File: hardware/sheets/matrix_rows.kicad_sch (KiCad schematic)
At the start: 0 parts

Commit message: hw: draw LED matrix, row and column drivers and scan-stall safety (#8)
* repo: ignore KiCad local history

KiCad 10 keeps automatic snapshots in a .history folder (with its own
Git repository) next to the project. Ignore it, and make the hygiene
check reject it, so local history cannot be committed.

* hw: save schematic sheets in KiCad's own format

Opening and saving the project in KiCad 10 rewrites the generated
sheets and project file in its native layout. KiCad also merges seven
overlapping wire segments on the USB sheet. Nets, values and
footprints are unchanged, so committing this once keeps later edits
made in KiCad free of formatting churn.

* hw: add column driver and monostable symbols

Add a TLC59283 symbol with the RGE (VQFN-24) pin numbers from TI's pin
table; it uses KiCad's footprint for TI's RGE0024C package. Add a
single-unit SN74LVC1G123 symbol, because KiCad's version keeps the
supply pins in a separate unit.

* hw: draw matrix driver and LED matrix sheets

Columns: two cascaded TLC59283 sinks on 3V3. R_IREF is 2.94k, an
18.0 mA nominal setting (about 19.4 mA worst case with driver and
resistor tolerance), with a fitted 0 ohm in series, so adjustment can
only lower the current.

Rows: the TLC chain output, clock, latch and SAFE cross into the LED
rail through an SN74LVC8T245 translator. Four SN74HC595 on VLED drive
32 AO3401A high-side switches with 10k gate pull-ups, with row
pull-downs as unfitted options.

Scan-stall safety: every latch retriggers an SN74LVC1G123. TI
specifies 1.0-1.1 ms at 10k / 0.1 uF; with the fitted parts'
tolerances the timeout is 0.76-1.41 ms. The part has only a Q
output, so an inverter makes SAFE = NOT Q. SAFE forces the column
BLANK through an OR gate and tri-states the row registers, and the
MCU reads it. The matrix stays dark while the MCU is off or in
reset.

LED matrix: 1024 LEDs, anodes on the rows and cathodes on the
columns, drawn as row and column buses, on the front side with the
buttons (ADR 0008).

The pend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
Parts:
- added C701, C702, C703, C704, C705, C706, C709, C710, C711, C712: 100nF, Capacitor_SMD:C_0402_1005Metric, symbol Device:C
- added C707, C708: 10uF 25V, Capacitor_SMD:C_0805_2012Metric, symbol Device:C
- added Q701, Q702, Q703, Q704, Q705, Q706, Q707, Q708, Q709, Q710, Q711, Q712, Q713, Q714, Q715, Q716, Q717, Q718, Q719, Q720, Q721, Q722, Q723, Q724, Q725, Q726, Q727, Q728, Q729, Q730, Q731, Q732: AO3401A, Package_TO_SOT_SMD:SOT-23, symbol Transistor_FET:AO3401A
- added R701: 0, Resistor_SMD:R_0402_1005Metric, symbol Device:R
- added R702: 10k, Resistor_SMD:R_0402_1005Metric, symbol Device:R
- added R703, R704, R705: 100k, Resistor_SMD:R_0402_1005Metric, symbol Device:R
- added RN701, RN702, RN703, RN704, RN705, RN706, RN707, RN708: 4x10k, Resistor_SMD:R_Array_Convex_4x0603, symbol Device:R_Pack04
- added RN709, RN710, RN711, RN712, RN713, RN714, RN715, RN716: DNP, Resistor_SMD:R_Array_Convex_4x0603, symbol Device:R_Pack04
- added TP701: MTX_BLANK, TestPoint:TestPoint_Pad_D1.0mm, symbol Connector:TestPoint
- added TP702: BLANK_TLC, TestPoint:TestPoint_Pad_D1.0mm, symbol Connector:TestPoint
- added TP703: MTX_SAFE_SENSE, TestPoint:TestPoint_Pad_D1.0mm, symbol Connector:TestPoint
- added TP704: SCAN_OK, TestPoint:TestPoint_Pad_D1.0mm, symbol Connector:TestPoint
- added TP705: SER_V, TestPoint:TestPoint_Pad_D1.0mm, symbol Connector:TestPoint
- added TP706: SRCLK_V, TestPoint:TestPoint_Pad_D1.0mm, symbol Connector:TestPoint
- added TP707: RCLK_V, TestPoint:TestPoint_Pad_D1.0mm, symbol Connector:TestPoint
- added TP708: ROW0, TestPoint:TestPoint_Pad_D1.0mm, symbol Connector:TestPoint
- added TP709: ROW16, TestPoint:TestPoint_Pad_D1.0mm, symbol Connector:TestPoint
- added TP710: ROW31, TestPoint:TestPoint_Pad_D1.0mm, symbol Connector:TestPoint
- added U701: SN74LVC8T245, Package_SO:TSSOP-24_4.4x7.8mm_P0.65mm, symbol Logic_LevelTranslator:SN74LVC8T245
- added U702, U703, U704, U705: SN74HC595, Package_SO:TSSOP-16_4.4x5mm_P0.65mm, symbol 74xx:74HC595
- added U706: SN74LVC1G123, Package_SO:SSOP-8_2.95x2.8mm_P0.65mm, symbol smart-led-badge:SN74LVC1G123
- added U707: SN74LVC1G04, Package_TO_SOT_SMD:SOT-23-5, symbol 74xGxx:74LVC1G04
- added U708: SN74LVC1G32, Package_TO_SOT_SMD:SOT-23-5, symbol 74xGxx:74LVC1G32
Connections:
- new net +3V3: C701.1, C710.1, C711.1, C712.1, R702.2, R704.2, U701.1 (V_{CCA}), U701.2 (DIR), U706.8 (VCC), U707.5 (VCC), U708.5 (VCC)
- new net BLANK_TLC: TP702.1, U708.4
- new net GND: C701.2, C702.2, C703.2, C704.2, C705.2, C706.2, C707.2, C708.2, C710.2, C711.2, C712.2, R701.2, R703.2, RN709.5 (R4.2), RN709.6 (R3.2), RN709.7 (R2.2), RN709.8 (R1.2), RN710.5 (R4.2), RN710.6 (R3.2), RN710.7 (R2.2), RN710.8 (R1.2), RN711.5 (R4.2), RN711.6 (R3.2), RN711.7 (R2.2), RN711.8 (R1.2), RN712.5 (R4.2), RN712.6 (R3.2), RN712.7 (R2.2), RN712.8 (R1.2), RN713.5 (R4.2), RN713.6 (R3.2), RN713.7 (R2.2), RN713.8 (R1.2), RN714.5 (R4.2), RN714.6 (R3.2), RN714.7 (R2.2), RN714.8 (R1.2), RN715.5 (R4.2), RN715.6 (R3.2), RN715.7 (R2.2), RN715.8 (R1.2), RN716.5 (R4.2), RN716.6 (R3.2), RN716.7 (R2.2), RN716.8 (R1.2), U701.10 (A8), U701.11 (GND), U701.12 (GND), U701.13 (GND), U701.7 (A5), U701.8 (A6), U701.9 (A7), U702.8 (GND), U703.8 (GND), U704.8 (GND), U705.8 (GND), U706.1 (~{A}), U706.4 (GND), U707.3 (GND), U708.3 (GND)
- new net MONO_CEXT: C709.1, U706.6 (Cext)
- new net MONO_RCEXT: C709.2, R702.1, U706.7 (Rext/Cext)
- new net MTX_ARM: R703.1, U706.3 (~{CLR})
- new net MTX_BLANK: R704.1, TP701.1, U708.1
- new net MTX_LAT: U701.5 (A3), U706.2 (B)
- new net MTX_MISO: U701.3 (A1)
- new net MTX_SAFE_SENSE: TP703.1, U701.6 (A4), U707.4, U708.2
- new net MTX_SCK: U701.4 (A2)
- new net OE_V: R705.1, U701.18 (B4), U702.13 (~{OE}), U703.13 (~{OE}), U704.13 (~{OE}), U705.13 (~{OE})
- new net RCLK_V: TP707.1, U701.19 (B3), U702.12 (RCLK), U703.12 (RCLK), U704.12 (RCLK), U705.12 (RCLK)
- new net RG0: Q701.1 (G), RN701.1 (R1.1), U702.15 (QA)
- new net RG1: Q702.1 (G), RN701.2 (R2.1), U702.1 (QB)
- new net RG10: Q711.1 (G), RN703.3 (R3.1), U703.2 (QC)
- new net RG11: Q712.1 (G), RN703.4 (R4.1), U703.3 (QD)
- new net RG12: Q713.1 (G), RN704.1 (R1.1), U703.4 (QE)
- new net RG13: Q714.1 (G), RN704.2 (R2.1), U703.5 (QF)
- new net RG14: Q715.1 (G), RN704.3 (R3.1), U703.6 (QG)
- new net RG15: Q716.1 (G), RN704.4 (R4.1), U703.7 (QH)
- new net RG16: Q717.1 (G), RN705.1 (R1.1), U704.15 (QA)
- new net RG17: Q718.1 (G), RN705.2 (R2.1), U704.1 (QB)
- new net RG18: Q719.1 (G), RN705.3 (R3.1), U704.2 (QC)
- new net RG19: Q720.1 (G), RN705.4 (R4.1), U704.3 (QD)
- new net RG2: Q703.1 (G), RN701.3 (R3.1), U702.2 (QC)
- new net RG20: Q721.1 (G), RN706.1 (R1.1), U704.4 (QE)
- new net RG21: Q722.1 (G), RN706.2 (R2.1), U704.5 (QF)
- new net RG22: Q723.1 (G), RN706.3 (R3.1), U704.6 (QG)
- new net RG23: Q724.1 (G), RN706.4 (R4.1), U704.7 (QH)
- new net RG24: Q725.1 (G), RN707.1 (R1.1), U705.15 (QA)
- new net RG25: Q726.1 (G), RN707.2 (R2.1), U705.1 (QB)
- new net RG26: Q727.1 (G), RN707.3 (R3.1), U705.2 (QC)
- new net RG27: Q728.1 (G), RN707.4 (R4.1), U705.3 (QD)
- new net RG28: Q729.1 (G), RN708.1 (R1.1), U705.4 (QE)
- new net RG29: Q730.1 (G), RN708.2 (R2.1), U705.5 (QF)
- new net RG3: Q704.1 (G), RN701.4 (R4.1), U702.3 (QD)
- new net RG30: Q731.1 (G), RN708.3 (R3.1), U705.6 (QG)
- new net RG31: Q732.1 (G), RN708.4 (R4.1), U705.7 (QH)
- new net RG4: Q705.1 (G), RN702.1 (R1.1), U702.4 (QE)
- new net RG5: Q706.1 (G), RN702.2 (R2.1), U702.5 (QF)
- new net RG6: Q707.1 (G), RN702.3 (R3.1), U702.6 (QG)
- new net RG7: Q708.1 (G), RN702.4 (R4.1), U702.7 (QH)
- new net RG8: Q709.1 (G), RN703.1 (R1.1), U703.15 (QA)
- new net RG9: Q710.1 (G), RN703.2 (R2.1), U703.1 (QB)
- new net ROW0: Q701.3 (D), RN709.1 (R1.1), TP708.1
- new net ROW1: Q702.3 (D), RN709.2 (R2.1)
- new net ROW10: Q711.3 (D), RN711.3 (R3.1)
- new net ROW11: Q712.3 (D), RN711.4 (R4.1)
- new net ROW12: Q713.3 (D), RN712.1 (R1.1)
- new net ROW13: Q714.3 (D), RN712.2 (R2.1)
- new net ROW14: Q715.3 (D), RN712.3 (R3.1)
- new net ROW15: Q716.3 (D), RN712.4 (R4.1)
- new net ROW16: Q717.3 (D), RN713.1 (R1.1), TP709.1
- new net ROW17: Q718.3 (D), RN713.2 (R2.1)
- new net ROW18: Q719.3 (D), RN713.3 (R3.1)
- new net ROW19: Q720.3 (D), RN713.4 (R4.1)
- new net ROW2: Q703.3 (D), RN709.3 (R3.1)
- new net ROW20: Q721.3 (D), RN714.1 (R1.1)
- new net ROW21: Q722.3 (D), RN714.2 (R2.1)
- new net ROW22: Q723.3 (D), RN714.3 (R3.1)
- new net ROW23: Q724.3 (D), RN714.4 (R4.1)
- new net ROW24: Q725.3 (D), RN715.1 (R1.1)
- new net ROW25: Q726.3 (D), RN715.2 (R2.1)
- new net ROW26: Q727.3 (D), RN715.3 (R3.1)
- new net ROW27: Q728.3 (D), RN715.4 (R4.1)
- new net ROW28: Q729.3 (D), RN716.1 (R1.1)
- new net ROW29: Q730.3 (D), RN716.2 (R2.1)
- new net ROW3: Q704.3 (D), RN709.4 (R4.1)
- new net ROW30: Q731.3 (D), RN716.3 (R3.1)
- new net ROW31: Q732.3 (D), RN716.4 (R4.1), TP710.1
- new net ROW4: Q705.3 (D), RN710.1 (R1.1)
- new net ROW5: Q706.3 (D), RN710.2 (R2.1)
- new net ROW6: Q707.3 (D), RN710.3 (R3.1)
- new net ROW7: Q708.3 (D), RN710.4 (R4.1)
- new net ROW8: Q709.3 (D), RN711.1 (R1.1)
- new net ROW9: Q710.3 (D), RN711.2 (R2.1)
- new net SCAN_OK: TP704.1, U706.5 (Q), U707.2
- new net SER1: U702.9 (QH'), U703.14 (SER)
- new net SER2: U703.9 (QH'), U704.14 (SER)
- new net SER3: U704.9 (QH'), U705.14 (SER)
- new net SER_V: TP705.1, U701.21 (B1), U702.14 (SER)
- new net SRCLK_V: TP706.1, U701.20 (B2), U702.11 (SRCLK), U703.11 (SRCLK), U704.11 (SRCLK), U705.11 (SRCLK)
- new net VLED: C702.1, C703.1, C704.1, C705.1, C706.1, C707.1, C708.1, Q701.2 (S), Q702.2 (S), Q703.2 (S), Q704.2 (S), Q705.2 (S), Q706.2 (S), Q707.2 (S), Q708.2 (S), Q709.2 (S), Q710.2 (S), Q711.2 (S), Q712.2 (S), Q713.2 (S), Q714.2 (S), Q715.2 (S), Q716.2 (S), Q717.2 (S), Q718.2 (S), Q719.2 (S), Q720.2 (S), Q721.2 (S), Q722.2 (S), Q723.2 (S), Q724.2 (S), Q725.2 (S), Q726.2 (S), Q727.2 (S), Q728.2 (S), Q729.2 (S), Q730.2 (S), Q731.2 (S), Q732.2 (S), R705.2, RN701.5 (R4.2), RN701.6 (R3.2), RN701.7 (R2.2), RN701.8 (R1.2), RN702.5 (R4.2), RN702.6 (R3.2), RN702.7 (R2.2), RN702.8 (R1.2), RN703.5 (R4.2), RN703.6 (R3.2), RN703.7 (R2.2), RN703.8 (R1.2), RN704.5 (R4.2), RN704.6 (R3.2), RN704.7 (R2.2), RN704.8 (R1.2), RN705.5 (R4.2), RN705.6 (R3.2), RN705.7 (R2.2), RN705.8 (R1.2), RN706.5 (R4.2), RN706.6 (R3.2), RN706.7 (R2.2), RN706.8 (R1.2), RN707.5 (R4.2), RN707.6 (R3.2), RN707.7 (R2.2), RN707.8 (R1.2), RN708.5 (R4.2), RN708.6 (R3.2), RN708.7 (R2.2), RN708.8 (R1.2), U701.23 (V_{CCB}), U701.24 (V_{CCB}), U702.10 (~{SRCLR}), U702.16 (VCC), U703.10 (~{SRCLR}), U703.16 (VCC), U704.10 (~{SRCLR}), U704.16 (VCC), U705.10 (~{SRCLR}), U705.16 (VCC)
- new net XLAT_OE_N: R701.1, U701.22 (~{OE})
- no-connect marks 0 -> 5
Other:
- note added: "Matrix row drivers and scan-stall safety (Rev A) - design notes Row chain: TLC chain SOUT (MTX_MISO), MTX_SCK, MTX_LAT and SAFE cross into the VLED domain through U701 (SN74LVC8T245, VCCA 3V3, VCCB VLED, DIR high = A to B). Its VCC isolation and Ioff keep 3V3 signals off the unpowered 595s when the LED rail is off. 4 x SN74HC595 on VLED (VCC 2-6 V) shift 32 row bits behind the 32 column bits; one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"

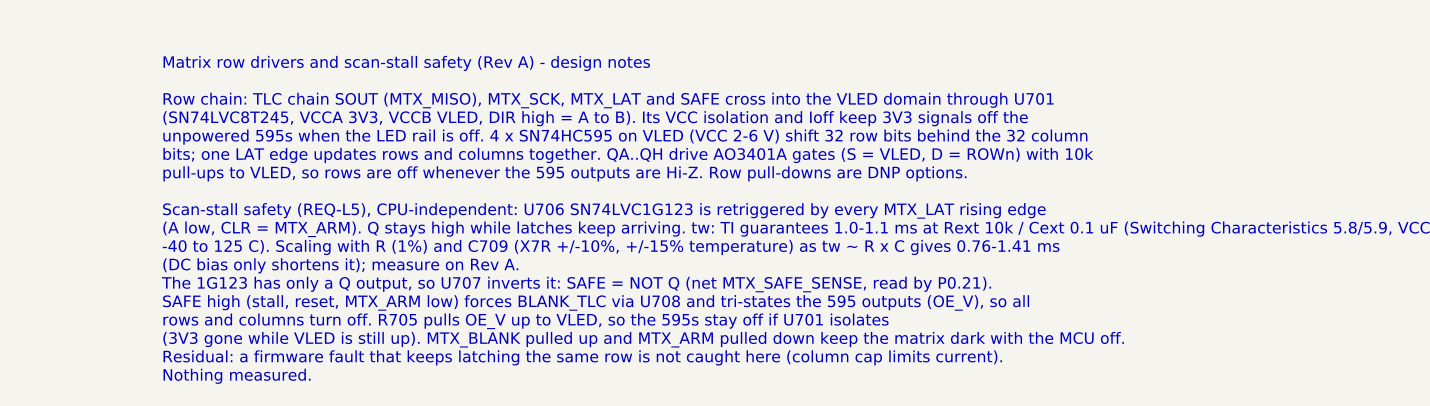
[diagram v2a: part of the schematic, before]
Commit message: hw: switch U401 to the E73 nRF52840 module
The MDBT53-P1M cannot be sourced in time for the Rev A order, while
the E73-2G4M08S1C is stocked at JLCPCB (ADR 0015).

The E73 holds its DC/DC inductors and decoupling, so L401/L402 and
C403/C404 are removed. The nRF52840 has no internal 32.768 kHz load,
so C405/C406 are fitted with 12 pF; the value is calculated and still
needs checking against the Product Specification. All 29 module GPIO
are used: CHG_STAT is no longer read by the MCU, and the UART pads,
spare GPIO pads and IMU SPI-fallback links are removed. Pins Ebyte
marks as low-frequency carry only analog inputs or slow signals.
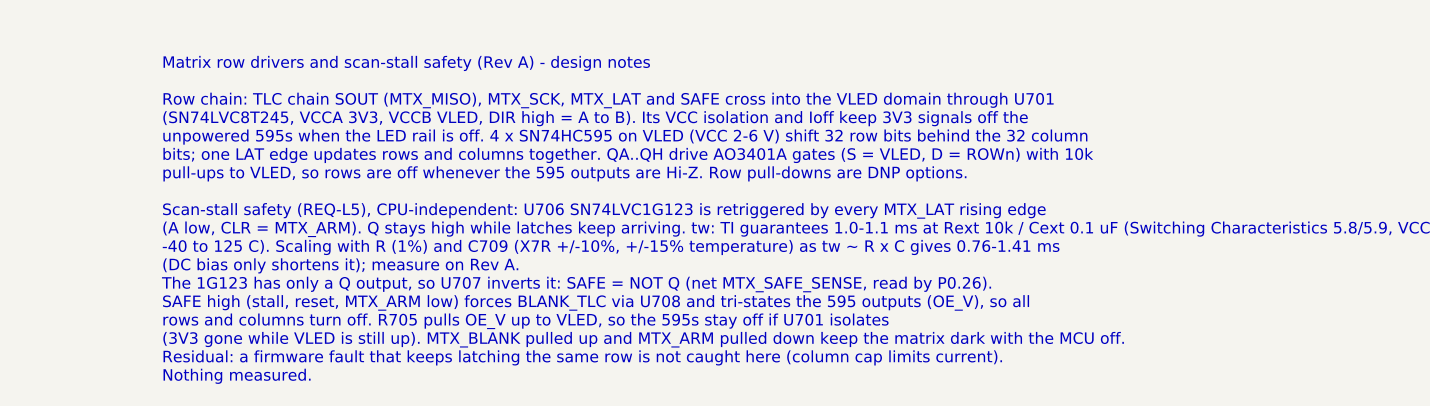
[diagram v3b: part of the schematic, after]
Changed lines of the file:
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@@
 		(comment 2 "Schematic frozen for layout after review 2026-10-07; not for fabrication until the release gate")
 	)
-	(text "Matrix row drivers and scan-stall safety (Rev A) - design notes\n\nRow chain: TLC chain SOUT (MTX_MISO), MTX_SCK, MTX_LAT and SAFE cross into the VLED domain through U701\n(SN74LVC8T245, VCCA 3V3, VCCB VLED, DIR high = A to B). Its VCC isolation and Ioff keep 3V3 signals off the\nunpowered 595s when the LED rail is off. 4 x SN74HC595 on VLED (VCC 2-6 V) shift 32 row bits behind the 32 column\nbits; one LAT edge updates rows and columns together. QA..QH drive AO3401A gates (S = VLED, D = ROWn) with 10k\npull-ups to VLED, so rows are off whenever the 595 outputs are Hi-Z. Row pull-downs are DNP options.\n\nScan-stall safety (REQ-L5), CPU-independent: U706 SN74LVC1G123 is retriggered by every MTX_LAT rising edge\n(A low, CLR = MTX_ARM). Q stays high while latches keep arriving. tw: TI guarantees 1.0-1.1 ms at Rext 10k / Cext 0.1 uF (Switching Characteristics 5.8/5.9, VCC 3.3 V,\n-40 to 125 C). Scaling with R (1%) and C709 (X7R +/-10%, +/-15% temperature) as tw ~ R x C gives 0.76-1.41 ms\n(DC bias only shortens it); measure on Rev A.\nThe 1G123 has only a Q output, so U707 inverts it: SAFE = NOT Q (net MTX_SAFE_SENSE, read by P0.21).\nSAFE high (stall, reset, MTX_ARM low) forces BLANK_TLC via U708 and tri-states the 595 outputs (OE_V), so all\nrows and columns turn off. R705 pulls OE_V up to VLED, so the 595s stay off if U701 isolates\n(3V3 gone while VLED is still up). MTX_BLANK pulled up and MTX_ARM pulled down keep the matrix dark with the MCU off.\nResidual: a firmware fault that keeps latching the same row is not caught here (column cap limits current).\nNothing measured."
+	(text "Matrix row drivers and scan-stall safety (Rev A) - design notes\n\nRow chain: TLC chain SOUT (MTX_MISO), MTX_SCK, MTX_LAT and SAFE cross into the VLED domain through U701\n(SN74LVC8T245, VCCA 3V3, VCCB VLED, DIR high = A to B). Its VCC isolation and Ioff keep 3V3 signals off the\nunpowered 595s when the LED rail is off. 4 x SN74HC595 on VLED (VCC 2-6 V) shift 32 row bits behind the 32 column\nbits; one LAT edge updates rows and columns together. QA..QH drive AO3401A gates (S = VLED, D = ROWn) with 10k\npull-ups to VLED, so rows are off whenever the 595 outputs are Hi-Z. Row pull-downs are DNP options.\n\nScan-stall safety (REQ-L5), CPU-independent: U706 SN74LVC1G123 is retriggered by every MTX_LAT rising edge\n(A low, CLR = MTX_ARM). Q stays high while latches keep arriving. tw: TI guarantees 1.0-1.1 ms at Rext 10k / Cext 0.1 uF (Switching Characteristics 5.8/5.9, VCC 3.3 V,\n-40 to 125 C). Scaling with R (1%) and C709 (X7R +/-10%, +/-15% temperature) as tw ~ R x C gives 0.76-1.41 ms\n(DC bias only shortens it); measure on Rev A.\nThe 1G123 has only a Q output, so U707 inverts it: SAFE = NOT Q (net MTX_SAFE_SENSE, read by P0.26).\nSAFE high (stall, reset, MTX_ARM low) forces BLANK_TLC via U708 and tri-states the 595 outputs (OE_V), so all\nrows and columns turn off. R705 pulls OE_V up to VLED, so the 595s stay off if U701 isolates\n(3V3 gone while VLED is still up). MTX_BLANK pulled up and MTX_ARM pulled down keep the matrix dark with the MCU off.\nResidual: a firmware fault that keeps latching the same row is not caught here (column cap limits current).\nNothing measured."
 		(exclude_from_sim no)
 		(at 50.8 360.68 0)

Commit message: hw: lay out and route the Rev A board (#29)
* hw: add fab-layer references to custom footprints

Show each part's reference on F.Fab so the assembly drawing used for
bring-up and rework labels the custom parts the same way as the KiCad
library parts. Copper, courtyards and silkscreen are unchanged.

* hw: join the NFC coil's twin pad-2 ends as a jumper

The coil's inner and outer pad-2 ends are connected by footprint copper
(the In1 crossover), which KiCad does not count as a connection, so
NFC_LB stayed unrouted. Treat the duplicate pad numbers as a jumper.
The pad 1/2 net tie is unchanged.

* hw: remove unfitted parts and spare test points

Free routing room on the Rev A board:
- remove the eight DNP row pull-down arrays (RN709-RN716) and six DNP
  passive positions (C1103, R1005, R1104, R212, R213, R310)
- remove 19 test points outside the required set that had no room on
  the routed board

No net changes and no fitted-part changes, so the assembled board and
its BOM are the same. C1102 stays as the DNP NFC tuning position.

* hw: lay out and route the Rev A board

Place and route the 118 x 76 mm four-layer board: the 32 x 32 matrix at
45 degrees on the west, the row drivers in a column beside it, and the
power, charger, NFC, IMU, microphone and E73 module on the east. In1 is
a GND plane kept solid under the regulators, charger and module; a few
low-current signals cross it elsewhere where no other layer had room.
The board uses the JLC04161H-7628 stack-up, tented vias and
0.45/0.2 mm minimum vias.

Add release silkscreen: battery polarity at J302 on both faces,
test-point net names (front where they fit, rear behind each pad),
orientation-independent control marks, the board name and a designer
monogram on the NFC coil.

DRC and schematic parity are clean. Nothing is measured yet: charger,
USB, matrix timing, RF and NFC tuning remain bring-up checks. The README
and hardware docs now give the 118 x 76 mm outline.

* hw: move three vias out of component pads

The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
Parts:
- removed RN709, RN710, RN711, RN712, RN713, RN714, RN715, RN716: DNP, Resistor_SMD:R_Array_Convex_4x0603, symbol Device:R_Pack04
- removed TP702: BLANK_TLC, TestPoint:TestPoint_Pad_D1.0mm, symbol Connector:TestPoint
- removed TP705: SER_V, TestPoint:TestPoint_Pad_D1.0mm, symbol Connector:TestPoint
- removed TP706: SRCLK_V, TestPoint:TestPoint_Pad_D1.0mm, symbol Connector:TestPoint
- removed TP707: RCLK_V, TestPoint:TestPoint_Pad_D1.0mm, symbol Connector:TestPoint
- removed TP710: ROW31, TestPoint:TestPoint_Pad_D1.0mm, symbol Connector:TestPoint
